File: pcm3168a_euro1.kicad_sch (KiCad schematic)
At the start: 39 parts, among them J8 Conn_01x02_Pin, U1 PCM3168APAPR

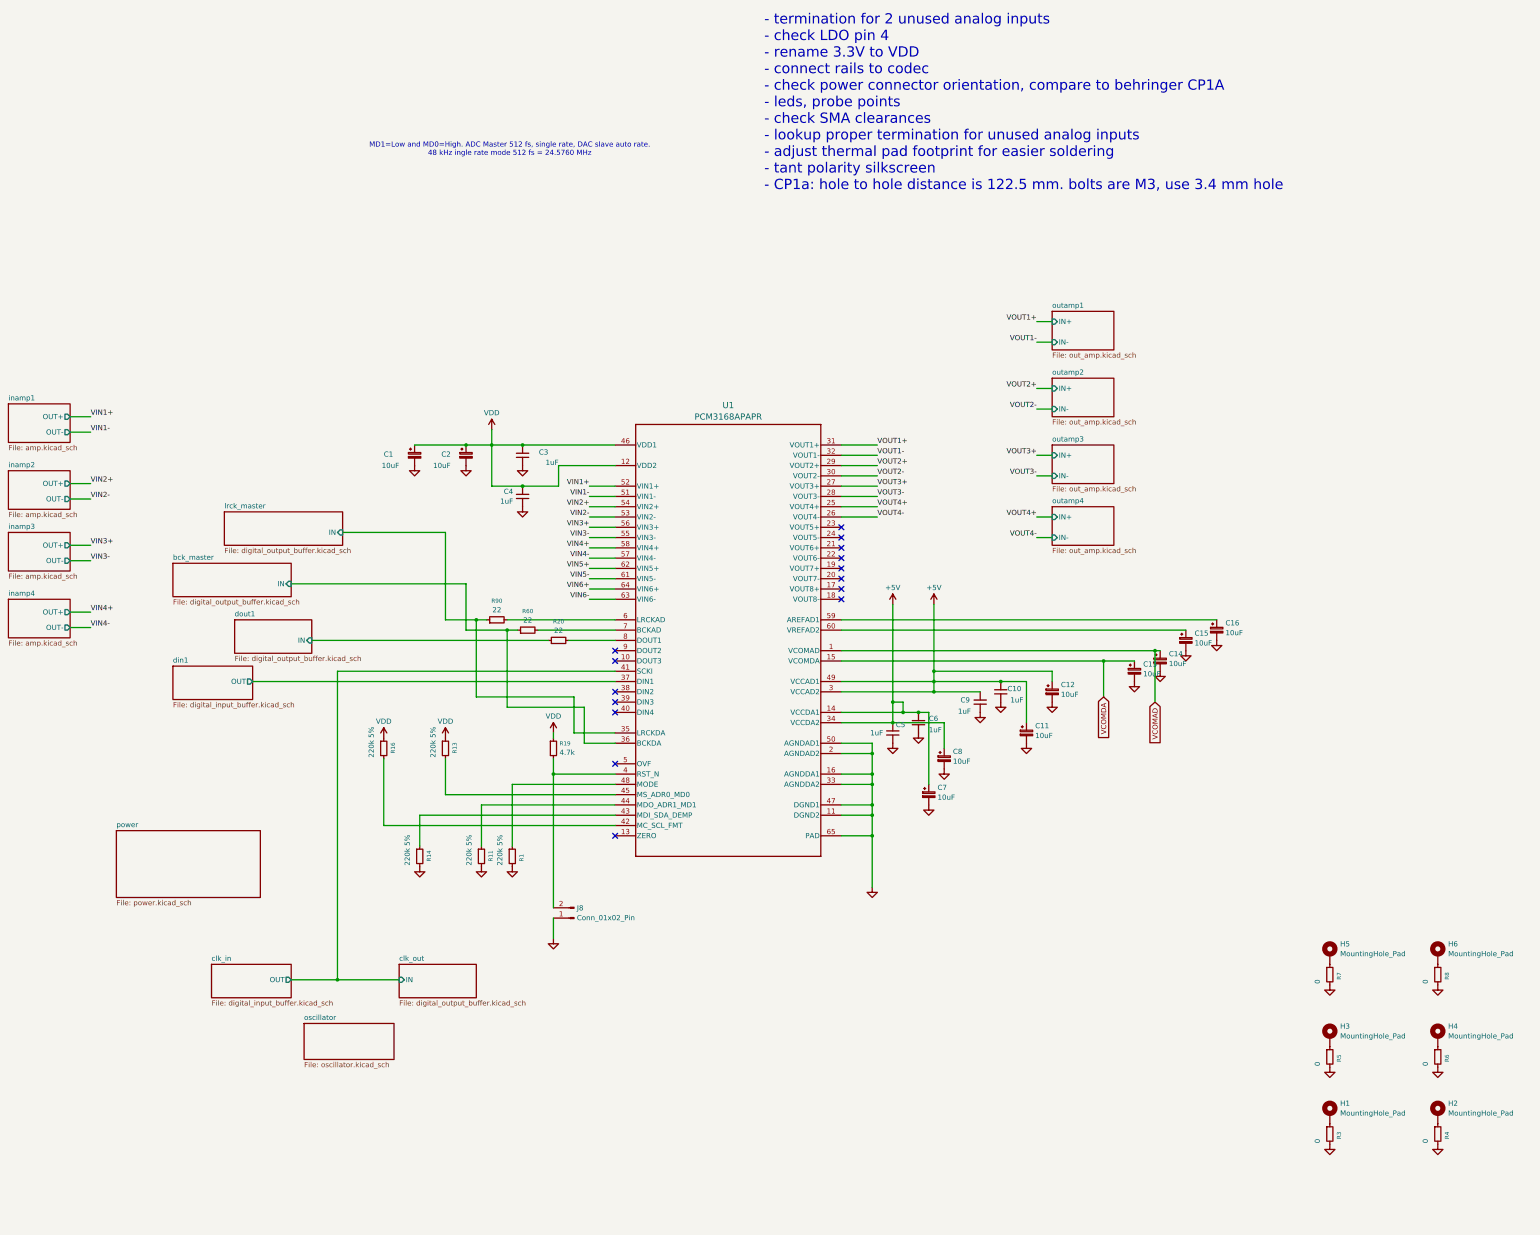
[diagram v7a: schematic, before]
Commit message: WIP need to fix OPA1637 footprint
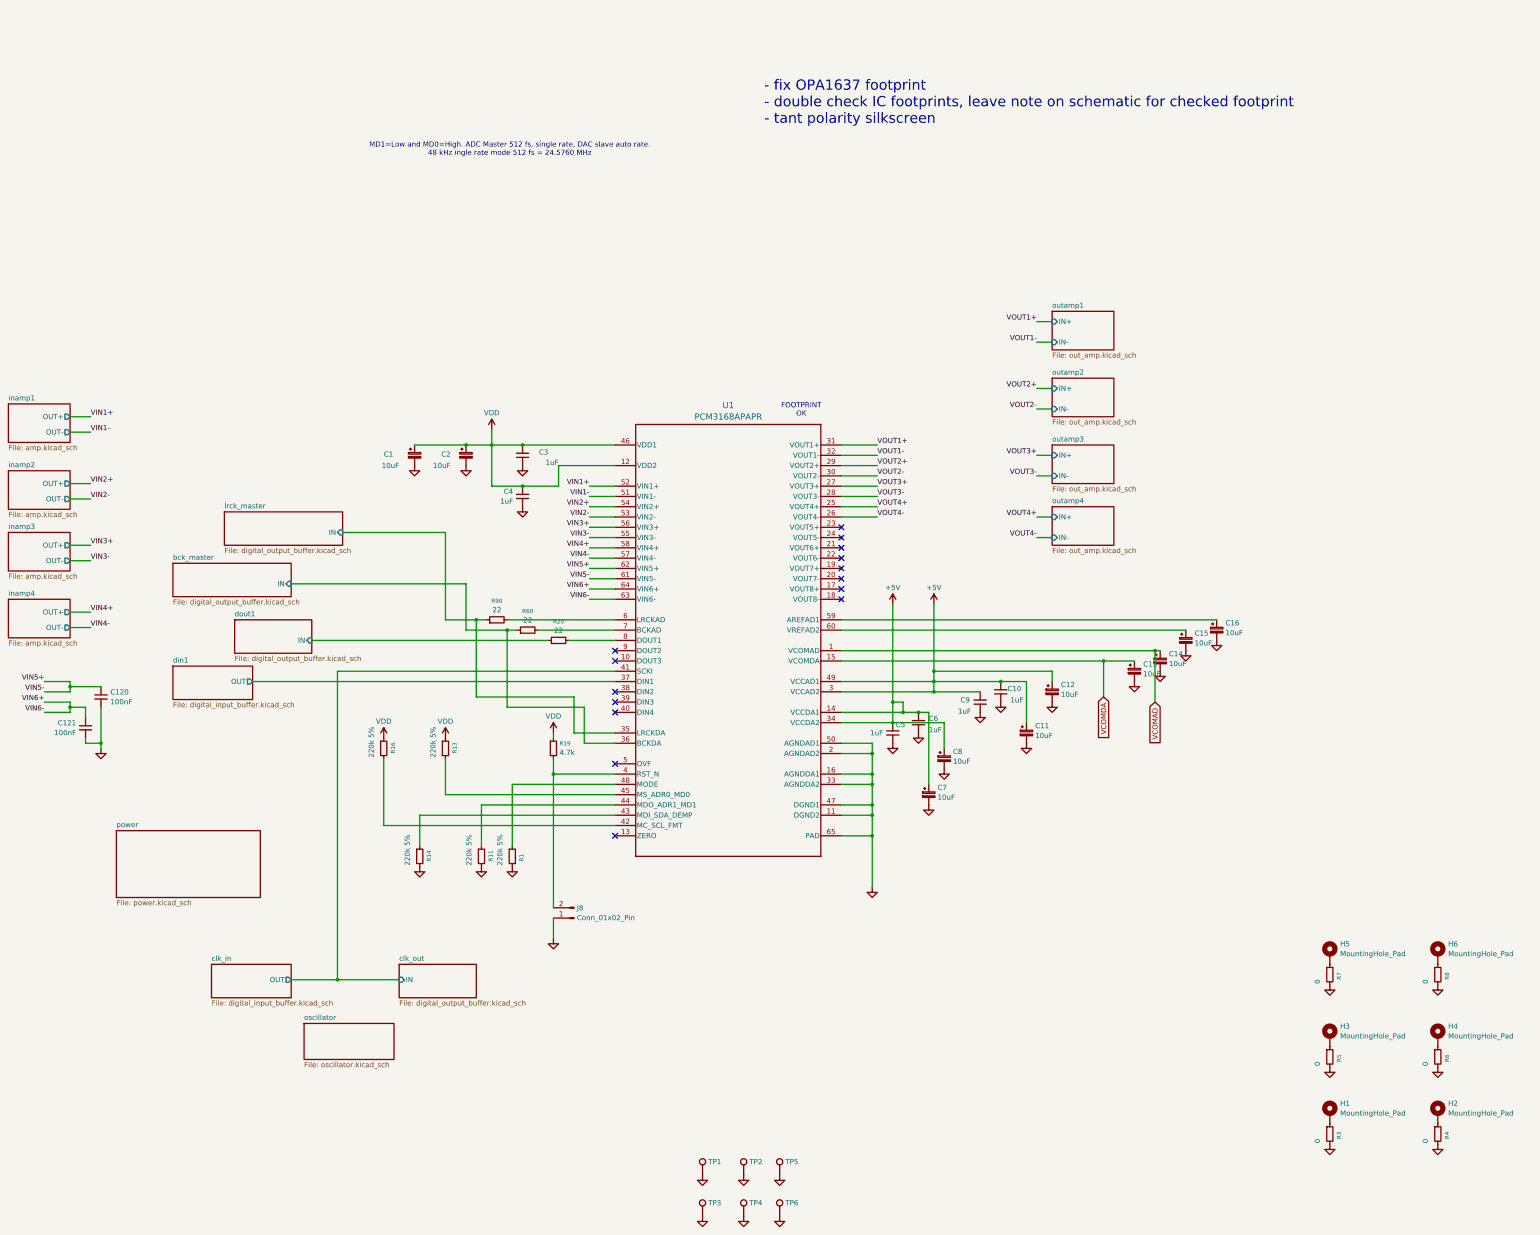
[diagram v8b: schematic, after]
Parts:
- added C120, C121: 100nF, Capacitor_SMD:C_0603_1608Metric, symbol Device:C_Small
- added TP1, TP2, TP3, TP4, TP5, TP6: TestPoint, TestPoint:TestPoint_THTPad_D1.5mm_Drill0.7mm, symbol Connector:TestPoint
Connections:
- net VIN5- is gone; now on net VIN5+: U1.61 (VIN5-)
- net VIN6- is gone; now on net VIN6+: U1.63 (VIN6-)
- net GND: now also C120.2, C121.2, TP1.1, TP2.1, TP3.1, TP4.1, TP5.1, TP6.1
- net VIN5+: now also C120.1
- net VIN6+: now also C121.1
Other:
- note added: "- fix OPA1637 footprint - double check IC footprints, leave note on schematic for checked footprint - tant polarity silkscreen"
- note added: "FOOTPRINT OK"
- note removed: "- termination for 2 unused analog inputs - check LDO pin 4 - rename 3.3V to VDD - connect rails to codec - check power connector orientation, compare to behringer CP1A - leds, probe points - check SMA clearances - lookup proper termination for unused analog inputs - adjust thermal pad footprint for easier soldering - tant polarity silkscreen - CP1a: hole to hole distance is 122.5 mm. bolts are M3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"
